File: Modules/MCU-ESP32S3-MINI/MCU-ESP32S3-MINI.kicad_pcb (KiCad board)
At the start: 4 copper layers, 11 parts, among them SW1 BOOT, SW2 RESET, U1 ESP32-S3-MINI-1-N8

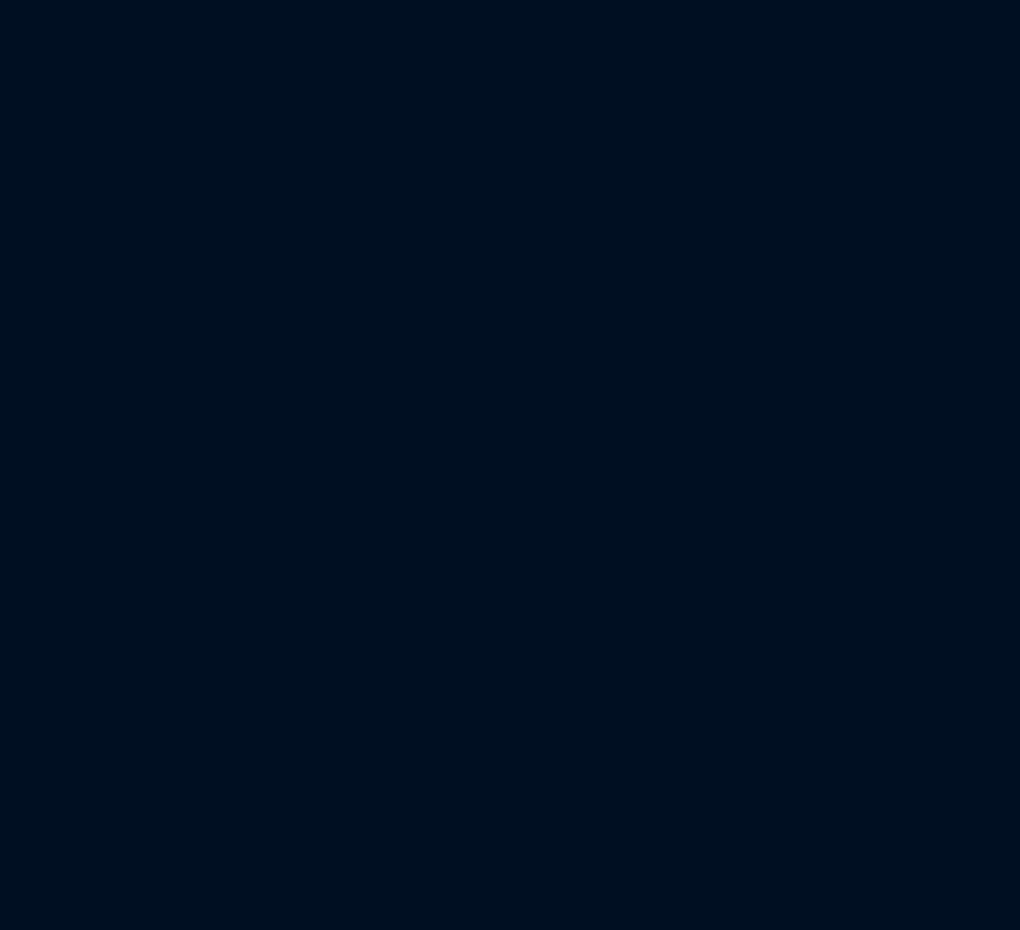
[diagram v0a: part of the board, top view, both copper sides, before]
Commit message: Add the base zones to five module boards
Whole-board zones for USBC, Buck, PowerMux, MCU and RF, written by file
before each board is opened. RF In1 carries a notch under J3 pad 1. Power
polygons become wide tracks during layout, because add_copper_pour cannot
set a zone priority.

Co-Authored-By: Claude Opus 5.5 (1M context) <noreply@anthropic.com>
Claude-Session: https://claude.ai/code/session_01ErAAfkmF4h3T5yfrw21utF
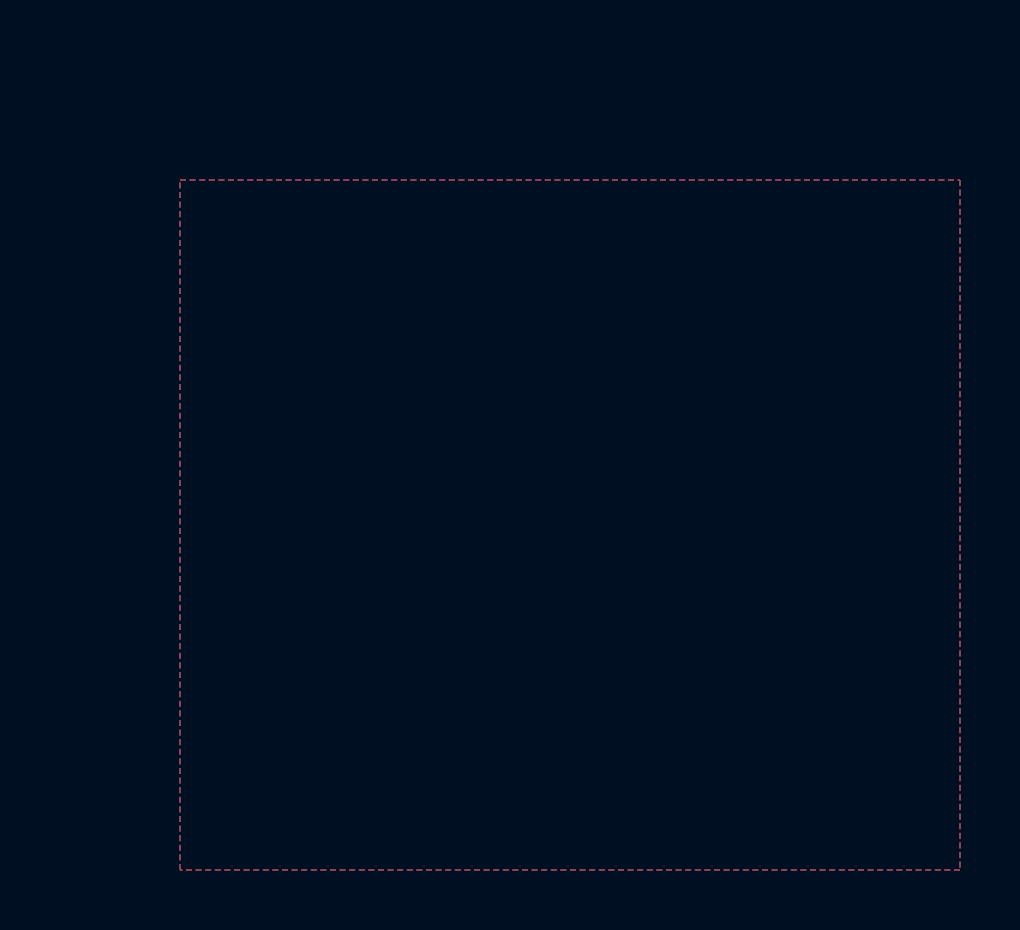
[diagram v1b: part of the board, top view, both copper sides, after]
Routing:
- added copper zone on In2.Cu, net +3V3
- added copper zone on B.Cu, net GND
- added copper zone on F.Cu, net GND
- added copper zone on In1.Cu, net GND
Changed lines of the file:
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@@
 	)
 	(embedded_fonts no)
-)
+  (zone (net 0) (net_name "GND") (layer "F.Cu")
+    (hatch edge 0.508)
+    (connect_pads (clearance 0.2))
+    (min_thickness 0.25)
+    (fill yes)
+    (polygon (pts
+      (xy 100.5 100.5)
+      (xy 126.5 100.5)
+      (xy 126.5 123.5)
+      (xy 100.5 123.5)
+    ))
+  )
+  (zone (net 0) (net_name "GND") (layer "In1.Cu")
+    (hatch edge 0.508)
+    (connect_pads (clearance 0.2))
+    (min_thickness 0.25)
+    (fill yes)
+    (polygon (pts
+      (xy 100.5 100.5)
+      (xy 126.5 100.5)
+      (xy 126.5 123.5)
+      (xy 100.5 123.5)
+    ))
+  )
+  (zone (net 0) (net_name "+3V3") (layer "In2.Cu")
+    (hatch edge 0.508)
+    (connect_pads (clearance 0.2))
+    (min_thickness 0.25)
+    (fill yes)
+    (polygon (pts
+      (xy 100.5 100.5)
+      (xy 126.5 100.5)
+      (xy 126.5 123.5)
+      (xy 100.5 123.5)
+    ))
+  )
+  (zone (net 0) (net_name "GND") (layer "B.Cu")
+    (hatch edge 0.508)
+    (connect_pads (clearance 0.2))
+    (min_thickness 0.25)
+    (fill yes)
+    (polygon (pts
+      (xy 100.5 100.5)
+      (xy 126.5 100.5)
+      (xy 126.5 123.5)
+      (xy 100.5 123.5)
+    ))
+  ))

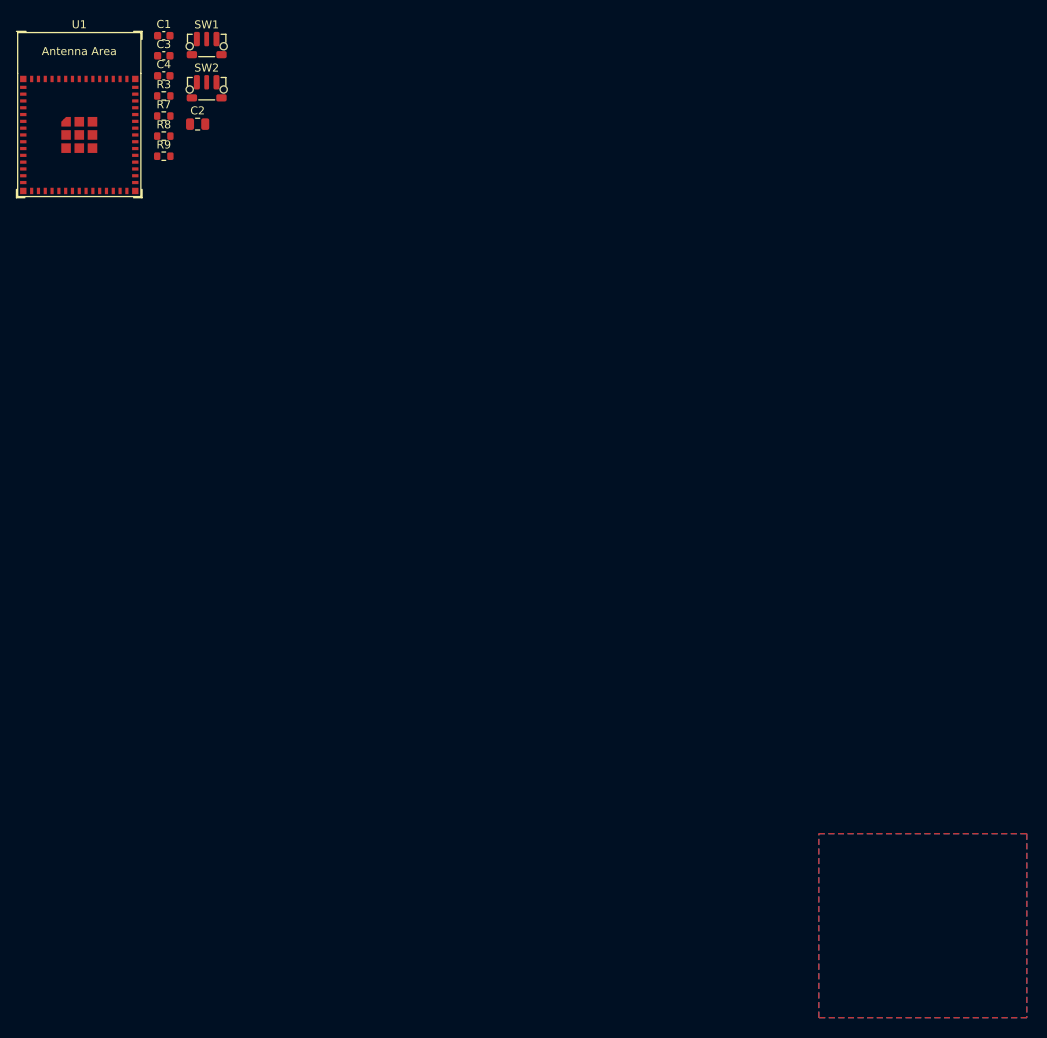
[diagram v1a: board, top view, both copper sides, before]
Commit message: Lay out the MCU-ESP32S3-MINI module
27 x 24 mm, 4 layers. U1 at the top-left corner with its antenna off the
board past the top edge, feed side 2.0 mm from the left edge (Espressif HDG
section 4.2). 12 GND thermal vias under the module. Two staggered breakout
rows on the bottom edge: 17 signals, the USB pair between GND guard vias,
two +3V3 vias.

Rules: pads 0.30 mm to the edge, the PCBWay figure the track rule already
uses. The Alps SKRTLAE010 land pattern gets an exception for each switch's
own pads and pegs.

DRC: 0 errors, 0 unconnected, 0 parity. The 17 track_dangling warnings are
the 17 interface stubs. Canary 47 to 535. Three lib_footprint_mismatch
warnings (U1, SW1, SW2): Konnect IPC writes drop the (units) block. GUI
batch 2 restores them from the library.

Co-Authored-By: Claude Opus 5.5 (1M context) <noreply@anthropic.com>
Claude-Session: https://claude.ai/code/session_01ErAAfkmF4h3T5yfrw21utF
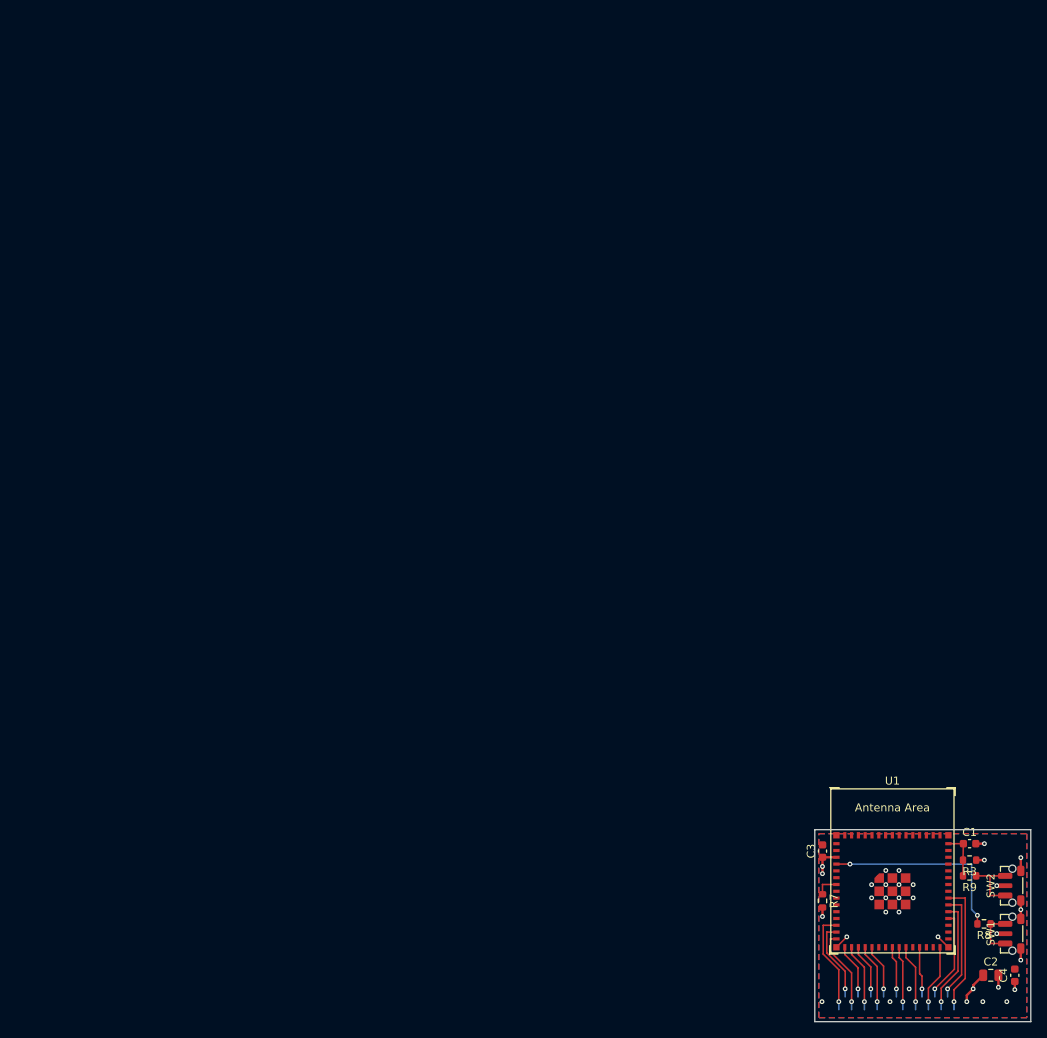
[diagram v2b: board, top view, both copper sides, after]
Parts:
- moved C4 154.8 mm to (125.0, 118.2), turned to 90 degrees
- moved SW1 149.8 mm to (124.7, 113.0), turned to 90 degrees
- moved C2 145.4 mm to (122.0, 118.2)
- moved C1 142.6 mm to (119.3, 101.8)
- moved R8 142.2 mm to (121.2, 111.8), turned to 180 degrees
- moved SW2 141.6 mm to (124.7, 107.0), turned to 90 degrees
- moved R3 138.8 mm to (119.3, 103.8), turned to 180 degrees
- moved U1 138.8 mm to (109.7, 107.7)
- moved R9 135.0 mm to (119.3, 105.8), turned to 180 degrees
- moved C3 129.1 mm to (101.0, 102.7), turned to 90 degrees
- moved R7 128.1 mm to (101.0, 108.9), turned to -90 degrees
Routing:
- net Net-(U1-IO0): track 0.00 -> 24.7 mm, vias 0 -> 2
- net /CC1101_CS: track 0.00 -> 16.6 mm, vias 0 -> 1
- net GND: track 0.00 -> 14.9 mm, vias 0 -> 27
- net /CC1101_MOSI: track 0.00 -> 14.3 mm, vias 0 -> 1
- net /CC1101_MISO: track 0.00 -> 13.9 mm, vias 0 -> 1
- net /ETH_RST: track 0.00 -> 13.0 mm, vias 0 -> 1
- net /CC1101_SCK: track 0.00 -> 11.6 mm, vias 0 -> 1
- net /ETH_MOSI: track 0.00 -> 10.7 mm, vias 0 -> 1
- net /ETH_CS: track 0.00 -> 10.3 mm, vias 0 -> 1
- net +3V3: track 0.00 -> 9.99 mm, vias 0 -> 6
- net /ETH_MISO: track 0.00 -> 8.46 mm, vias 0 -> 1
- net /CC1101_GDO0_TX: track 0.00 -> 8.42 mm, vias 0 -> 1
- net /LED_FAULT: track 0.00 -> 8.40 mm, vias 0 -> 1
- net /LED_RF_TX: track 0.00 -> 8.30 mm, vias 0 -> 1
- net /USB_DP: track 0.00 -> 7.99 mm, vias 0 -> 1
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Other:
- board outline added: 27 x 24 mm
- board text added: "+3V3"
- board text added: "CC1101_CS"
- board text added: "CC1101_GDO0_TX"
- board text added: "CC1101_GDO2_RX"
- board text added: "CC1101_MISO"
- board text added: "CC1101_MOSI"
- board text added: "CC1101_SCK"
- board text added: "ETH_CLK"
- board text added: "ETH_CS"
- board text added: "ETH_INT"
- board text added: "ETH_MISO"
- board text added: "ETH_MOSI"
- board text added: "ETH_RST"
- board text added: "GND"
- board text added: "LED_FAULT"
- board text added: "LED_LEARN"
- board text added: "LED_RF_TX"
- board text added: "USB_DM"
- board text added: "USB_DP"

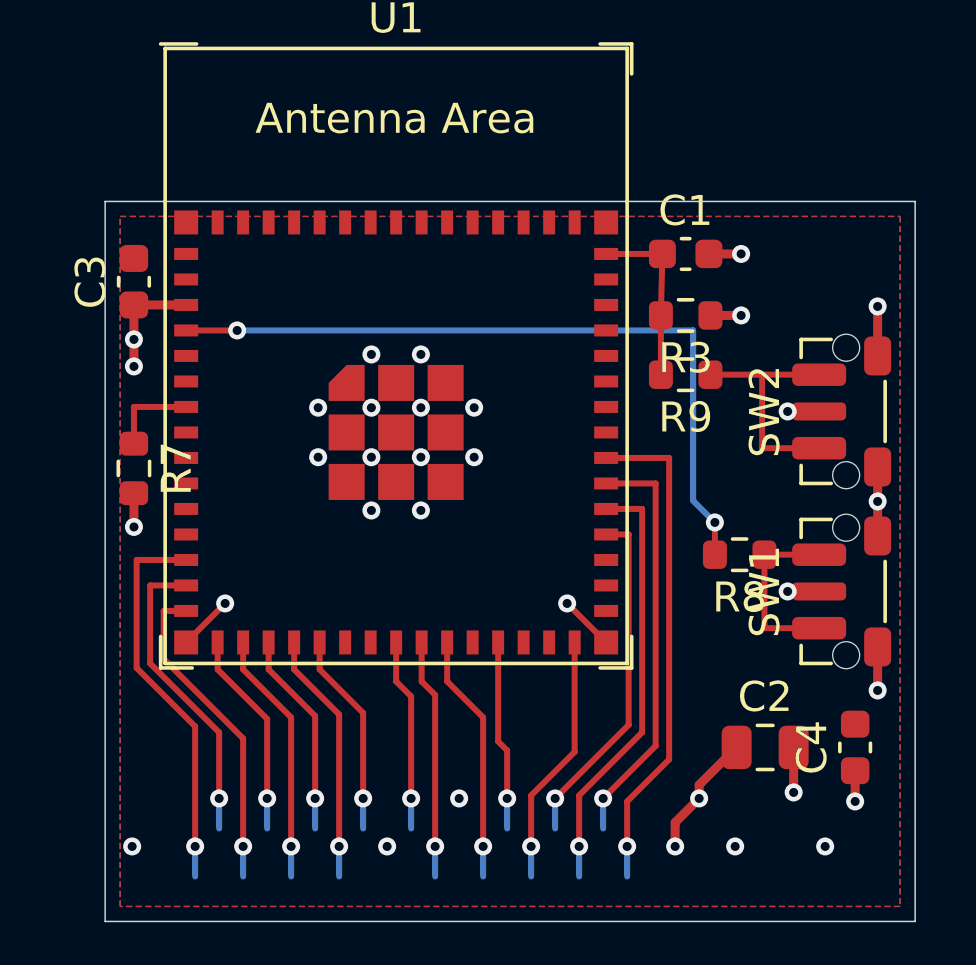
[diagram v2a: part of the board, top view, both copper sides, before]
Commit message: Restore footprints and move passive references to F.Fab
GUI batch 2a on all eight module boards. Update Footprints from Library
restores the (units) blocks that Konnect IPC writes dropped: U10, U1, SW1,
SW2 and U4 no longer report lib_footprint_mismatch. Reference designators of
C, R, L, FB, D, Y and TP parts move to F.Fab. U, J and SW stay on the silk.

Every board: DRC 0 errors, 0 unconnected, 0 parity, the canary fires, and
track_dangling equals the interface stub count.

Co-Authored-By: Claude Opus 5.5 (1M context) <noreply@anthropic.com>
Claude-Session: https://claude.ai/code/session_01ErAAfkmF4h3T5yfrw21utF
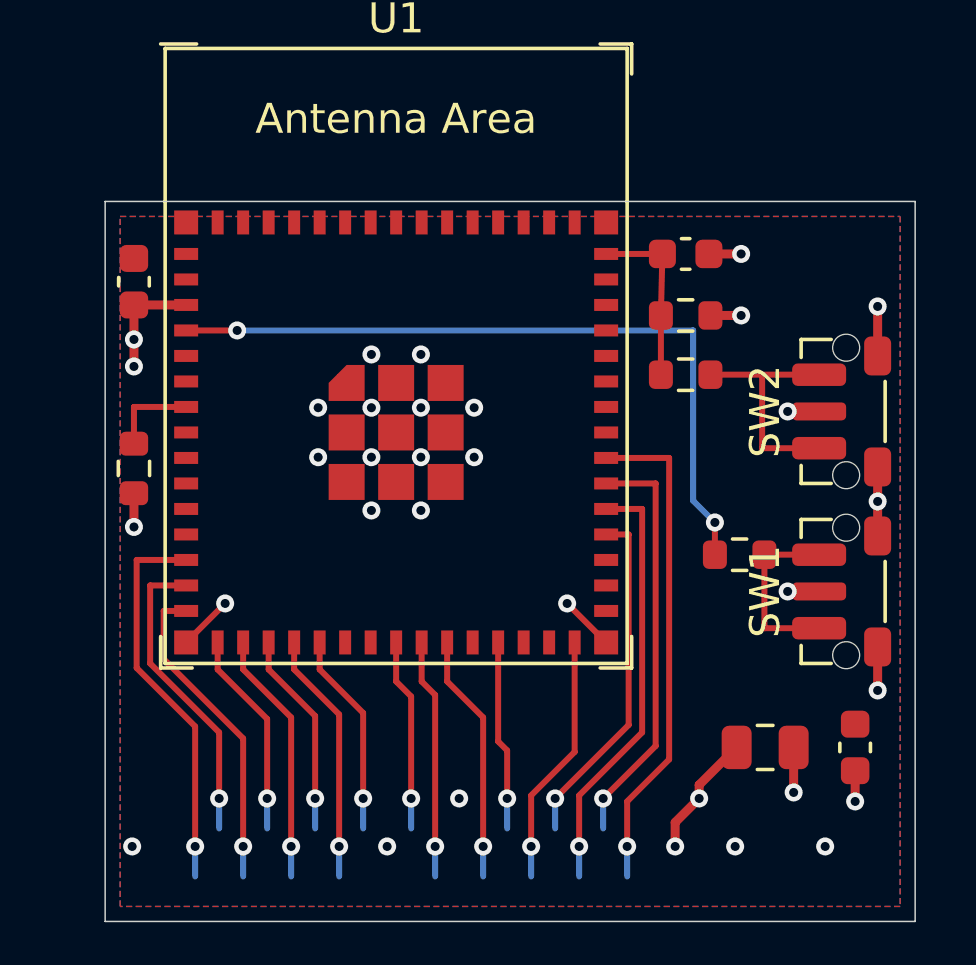
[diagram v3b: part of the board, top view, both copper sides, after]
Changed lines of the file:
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@@
 		(property "Reference" "R3"
 			(at 0 -1.43 180)
-			(layer "F.SilkS")
+			(layer "F.Fab")
 			(effects
 				(font
@@
 		(tags "push horizontal SPST 1P1T")
 		(property "Reference" "SW2"
-			(at 0 -2.7 -90)
+			(at 0 -2.7 270)
 			(layer "F.SilkS")
 			(effects
@@
 				(clearance 0)
 			)
-			(min_thickness 0.25)
+			(min_thickness 0.254)
 			(keepout
 				(tracks not_allowed)
@@
 			)
 			(fill
-				(thermal_gap 0.5)
-				(thermal_bridge_width 0.5)
+				(thermal_gap 0.508)
+				(thermal_bridge_width 0.508)
 				(island_removal_mode 0)
 			)
@@
 				(clearance 0)
 			)
-			(min_thickness 0.25)
+			(min_thickness 0.254)
 			(keepout
 				(tracks allowed)
@@
 			)
 			(fill
-				(thermal_gap 0.5)
-				(thermal_bridge_width 0.5)
+				(thermal_gap 0.508)
+				(thermal_bridge_width 0.508)
 				(island_removal_mode 0)
 			)
@@
 		(tags "resistor")
 		(property "Reference" "R7"
-			(at 0 -1.43 -90)
-			(layer "F.SilkS")
+			(at 0 -1.43 270)
+			(layer "F.Fab")
 			(effects
 				(font
@@
 		)
 		(property "Value" "10k"
-			(at 0 1.43 -90)
+			(at 0 1.43 270)
 			(layer "F.Fab")
 			(effects
@@
 		)
 		(property "Datasheet" ""
-			(at 0 0 -90)
+			(at 0 0 270)
 			(layer "F.Fab")
 			(hide yes)
@@
 		)
 		(property "Description" ""
-			(at 0 0 -90)
+			(at 0 0 270)
 			(layer "F.Fab")
 			(hide yes)
@@
 		)
 		(property "KiLib_Generator" "SMD_2terminal_chip_molded"
-			(at 0 0 -90)
+			(at 0 0 270)
 			(layer "F.SilkS")
 			(hide yes)
@@
 		)
 		(property "MPN" "RC0603FR-0710KL"
-			(at 0 0 -90)
+			(at 0 0 270)
 			(unlocked yes)
 			(layer "F.Fab")
@@
 		)
 		(property "Manufacturer" "Yageo"
-			(at 0 0 -90)
+			(at 0 0 270)
 			(unlocked yes)
 			(layer "F.Fab")
@@
 		)
 		(fp_text user "${REFERENCE}"
-			(at 0 0 -90)
+			(at 0 0 270)
 			(layer "F.Fab")
 			(effects
@@
 				(clearance 0)
 			)
-			(min_thickness 0.25)
+			(min_thickness 0.254)
 			(keepout
 				(tracks not_allowed)
@@
 			)
 			(fill
-				(thermal_gap 0.5)
-				(thermal_bridge_width 0.5)
+				(thermal_gap 0.508)
+				(thermal_bridge_width 0.508)
 				(island_removal_mode 0)
 			)
@@
 		(property "Reference" "C1"
 			(at 0 -1.43 0)
-			(layer "F.SilkS")
+			(layer "F.Fab")
 			(effects
 				(font
@@
 		(property "Reference" "C3"
 			(at 0 -1.43 90)
-			(layer "F.SilkS")
+			(layer "F.Fab")
 			(effects
 				(font
@@
 		(property "Reference" "R9"
 			(at 0 -1.43 180)
-			(layer "F.SilkS")
+			(layer "F.Fab")
 			(effects
 				(font
@@
 		(property "Reference" "C4"
 			(at 0 -1.43 90)
-			(layer "F.SilkS")
+			(layer "F.Fab")
 			(effects
 				(font
@@
 		(property "Reference" "C2"
 			(at 0 -1.68 0)
-			(layer "F.SilkS")
+			(layer "F.Fab")
 			(effects
 				(font
@@
 		(tags "push horizontal SPST 1P1T")
 		(property "Reference" "SW1"
-			(at 0 -2.7 -90)
+			(at 0 -2.7 270)
 			(layer "F.SilkS")
 			(effects
@@
 				(clearance 0)
 			)
-			(min_thickness 0.25)
+			(min_thickness 0.254)
 			(keepout
 				(tracks not_allowed)
@@
 			)
 			(fill
-				(thermal_gap 0.5)
-				(thermal_bridge_width 0.5)
+				(thermal_gap 0.508)
+				(thermal_bridge_width 0.508)
 				(island_removal_mode 0)
 			)
@@
 				(clearance 0)
 			)
-			(min_thickness 0.25)
+			(min_thickness 0.254)
 			(keepout
 				(tracks allowed)
@@
 			)
 			(fill
-				(thermal_gap 0.5)
-				(thermal_bridge_width 0.5)
+				(thermal_gap 0.508)
+				(thermal_bridge_width 0.508)
 				(island_removal_mode 0)
 			)
@@
 		(property "Reference" "R8"
 			(at 0 -1.43 180)
-			(layer "F.SilkS")
-			(effects
-				(font
+			(layer "F.Fab")
+			(effects
+				(font
